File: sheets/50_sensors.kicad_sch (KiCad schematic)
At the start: 0 parts

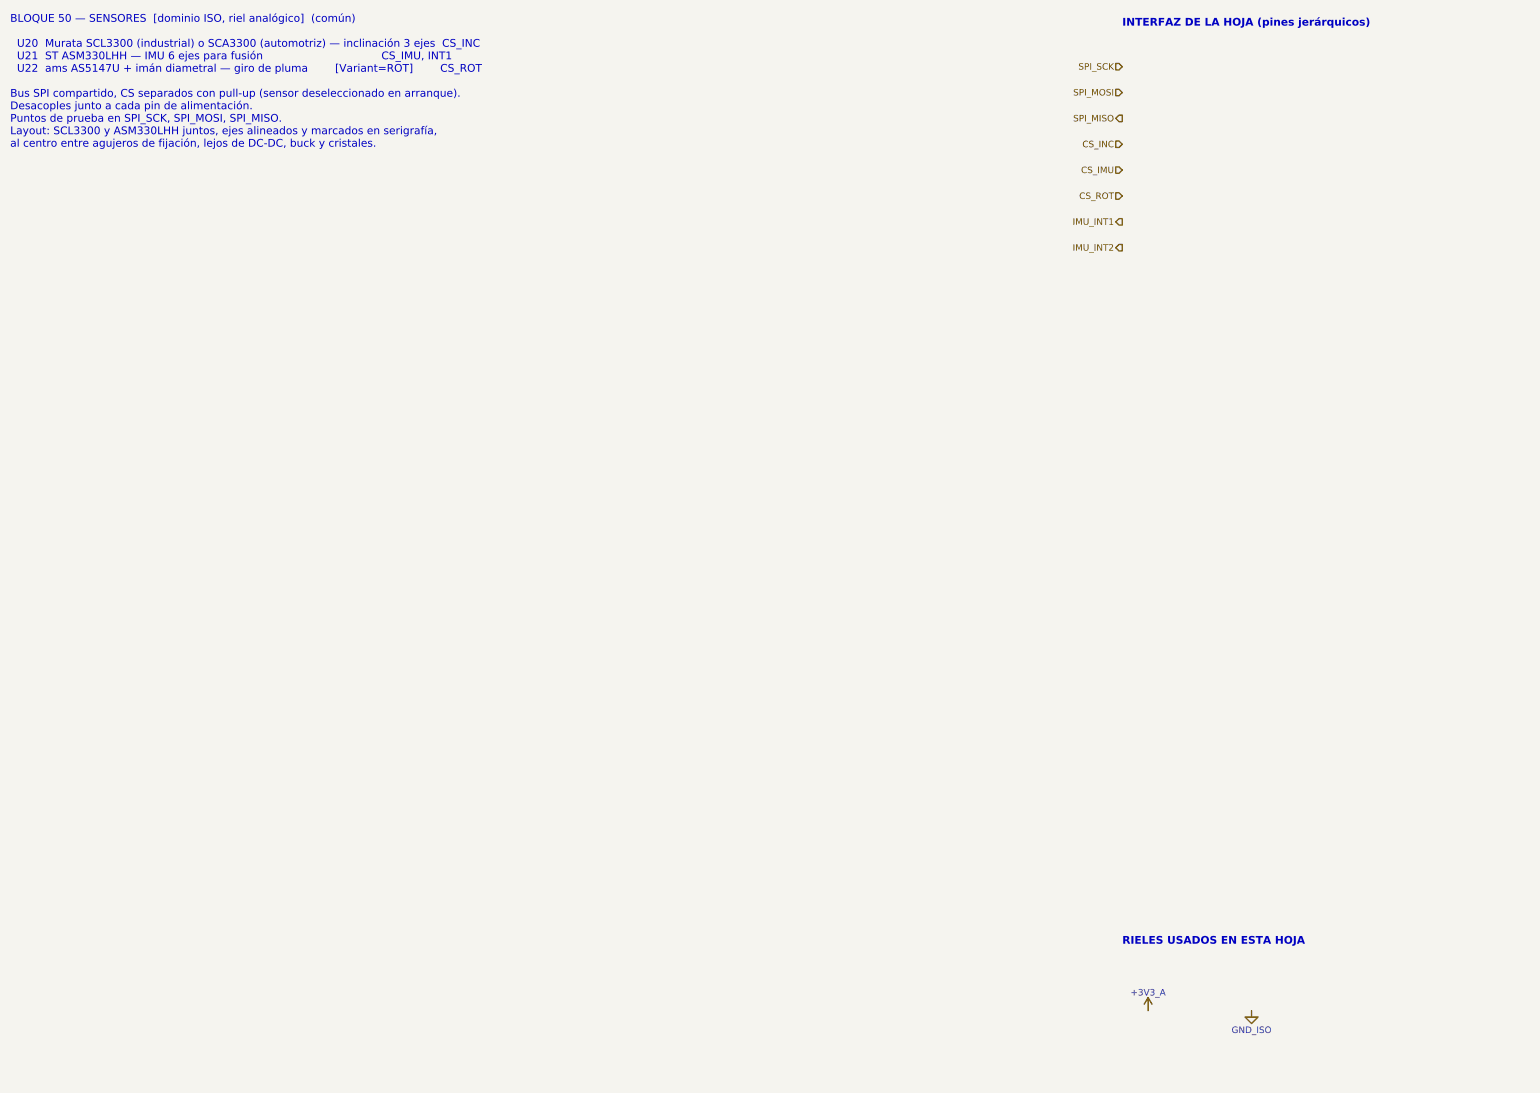
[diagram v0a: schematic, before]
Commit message: [Claude Code] 50_sensors: SCL3300-D01, ASM330LHH, AS5147U (ROT) en SPI compartido (fase 5)
- U501 SCL3300-D01: 4 x 100 nF (VDD, A_EXTC, D_EXTC, DVIO) según Murata
  Doc. 4921 fig. 16 / tabla 48. SPI modo 0, <= 8 MHz.
- U502 ASM330LHHTR (LGA, aire caliente): 100 nF + 10 uF en VDD y 100 nF en
  VDDIO (ST fig. 14); INT1/INT2 a IMU_INT1/2. SPI modo 3, <= 10 MHz.
- U503 AS5147U-HTSM: solo variante ROT (DNP en estándar junto con C507 y
  R503, campo Variant = ROT). SPI modo 1, <= 10 MHz.
- Pull-ups de 10 k a +3V3_A en los tres CS; TP de SCK, MOSI, MISO e INT1.
- Notas de layout: SCL3300 junto a las fijaciones y lejos del calor, ejes
  en serigrafía, placa centrada sobre el pivote en la variante ROT.
- Símbolos easyeda2kicad (C22416657, C459826, C38675951) con tipos de pin,
  fabricante y datasheet corregidos; huellas oficiales LGA-14 y TSSOP-14,
  DFL-12 de EasyEDA para el SCL3300 (comparada con la fig. 11 de Murata).
- Datasheets en docs/datasheets. ERC 0 en 50 (66 en el proyecto);
  sch_visual_qa PASS.
- docs/PENDIENTES.md: modos SPI para el firmware y nota de compra.

Co-Authored-By: Claude Opus 5.5 <noreply@anthropic.com>
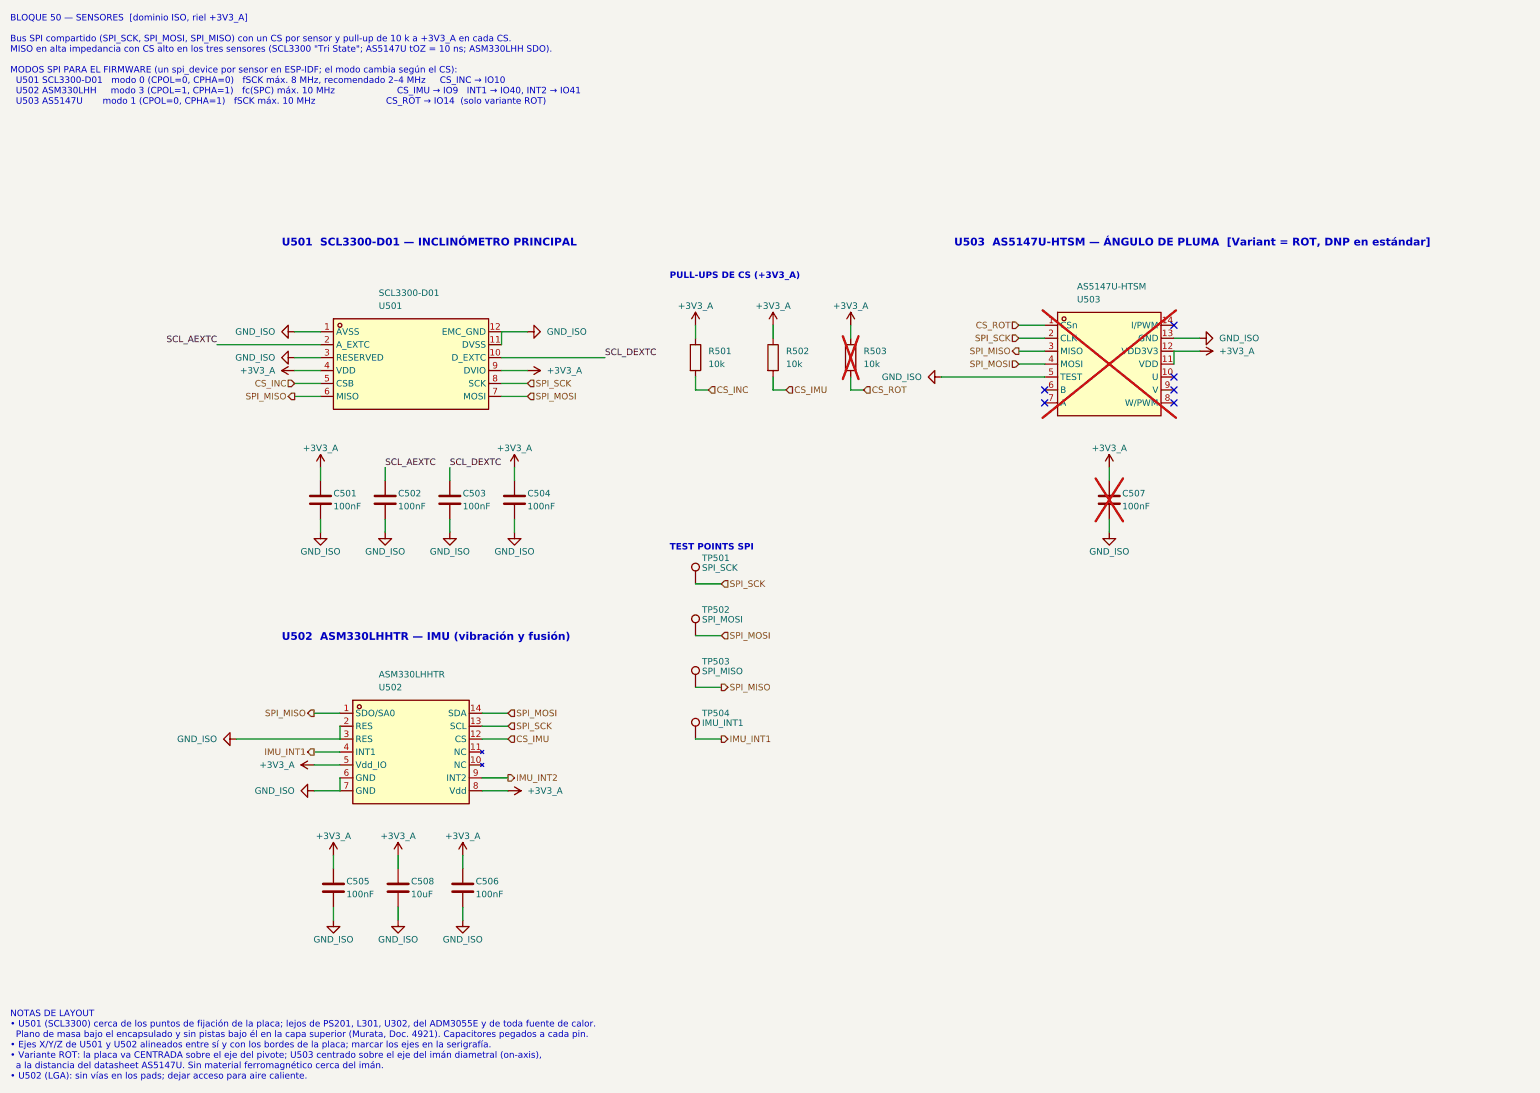
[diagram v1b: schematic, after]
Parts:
- added C501, C502, C503, C504, C505, C506, C507: 100nF, Capacitor_SMD:C_0603_1608Metric, symbol Device:C
- added C508: 10uF, Capacitor_SMD:C_0805_2012Metric, symbol Device:C
- added R501, R502, R503: 10k, Resistor_SMD:R_0603_1608Metric, symbol Device:R
- added TP501: SPI_SCK, TestPoint:TestPoint_Pad_D1.5mm, symbol Connector:TestPoint
- added TP502: SPI_MOSI, TestPoint:TestPoint_Pad_D1.5mm, symbol Connector:TestPoint
- added TP503: SPI_MISO, TestPoint:TestPoint_Pad_D1.5mm, symbol Connector:TestPoint
- added TP504: IMU_INT1, TestPoint:TestPoint_Pad_D1.5mm, symbol Connector:TestPoint
- added U501: SCL3300-D01, easyeda2kicad:DFL-12_L8.6-W7.0-P1.00-LS7.6-BL, symbol easyeda2kicad:SCL3300-D01
- added U502: ASM330LHHTR, Package_LGA:LGA-14_3x2.5mm_P0.5mm_LayoutBorder3x4y, symbol easyeda2kicad:ASM330LHHTR
- added U503: AS5147U-HTSM, Package_SO:TSSOP-14_4.4x5mm_P0.65mm, symbol easyeda2kicad:AS5147U-HTSM_C38675951
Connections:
- net +3V3_A: now also C501.1, C504.1, C505.1, C506.1, C507.1, C508.1, R501.1, R502.1, R503.1, U501.4 (VDD), U501.9 (DVIO), U502.5 (Vdd_IO), U502.8 (Vdd), U503.11 (VDD), U503.12 (VDD3V3)
- net CS_IMU: now also R502.2, U502.12 (CS)
- net CS_INC: now also R501.2, U501.5 (CSB)
- net CS_ROT: now also R503.2, U503.1 (CSn)
- net GND_ISO: now also C501.2, C502.2, C503.2, C504.2, C505.2, C506.2, C507.2, C508.2, U501.1 (AVSS), U501.11 (DVSS), U501.12 (EMC_GND), U501.3 (RESERVED), U502.2 (RES), U502.3 (RES), U502.6 (GND), U502.7 (GND), U503.13 (GND), U503.5 (TEST)
- net IMU_INT1: now also TP504.1, U502.4 (INT1)
- net IMU_INT2: now also U502.9 (INT2)
- net SPI_MISO: now also TP503.1, U501.6 (MISO), U502.1 (SDO/SA0), U503.3 (MISO)
- net SPI_MOSI: now also TP502.1, U501.7 (MOSI), U502.14 (SDA), U503.4 (MOSI)
- net SPI_SCK: now also TP501.1, U501.8 (SCK), U502.13 (SCL), U503.2 (CLK)
- new net SCL_AEXTC: C502.1, U501.2 (A_EXTC)
- new net SCL_DEXTC: C503.1, U501.10 (D_EXTC)
- no-connect marks 0 -> 6
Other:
- note added: "BLOQUE 50 — SENSORES [dominio ISO, riel +3V3_A] Bus SPI compartido (SPI_SCK, SPI_MOSI, SPI_MISO) con un CS por sensor y pull-up de 10 k a +3V3_A en cada CS. MISO en alta impedancia con CS alto en los tres sensores (SCL3300 "Tri State"; AS5147U tOZ = 10 ns; ASM330LHH SDO). MODOS SPI PARA EL FIRMWARE (un spi_device por sensor en ESP-IDF; el modo cambia según el CS): U501 SCL3300-D01 modo 0 (CPOL=0,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"
- note added: "NOTAS DE LAYOUT • U501 (SCL3300) cerca de los puntos de fijación de la placa; lejos de PS201, L301, U302, del ADM3055E y de toda fuente de calor. Plano de masa bajo el encapsulado y sin pistas bajo él en la capa superior (Murata, Doc. 4921). Capacitores pegados a cada pin. • Ejes X/Y/Z de U501 y U502 alineados entre sí y con los bordes de la placa; marcar los ejes en la serigrafía. • Variante ROT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"
- note added: "PULL-UPS DE CS (+3V3_A)"
- note added: "TEST POINTS SPI"
- note added: "U501 SCL3300-D01 — INCLINÓMETRO PRINCIPAL"
- note added: "U502 ASM330LHHTR — IMU (vibración y fusión)"
- note added: "U503 AS5147U-HTSM — ÁNGULO DE PLUMA [Variant = ROT, DNP en estándar]"
- note removed: "BLOQUE 50 — SENSORES [dominio ISO, riel analógico] (común) U20 Murata SCL3300 (industrial) o SCA3300 (automotriz) — inclinación 3 ejes CS_INC U21 ST ASM330LHH — IMU 6 ejes para fusión CS_IMU, INT1 U22 ams AS5147U + imán diametral — giro de pluma [Variant=ROT] CS_ROT Bus SPI compartido, CS separados con pull-up (sensor deseleccionado en arranque). Desacoples junto a cada pin de alimentación. Punto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"
- note removed: "INTERFAZ DE LA HOJA (pines jerárquicos)"
- note removed: "RIELES USADOS EN ESTA HOJA"
